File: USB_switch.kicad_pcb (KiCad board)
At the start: 2 copper layers, 29 x 44 mm, 20 parts, among them Q1 Q_PMOS_GSD, SW1 SW_SPDT

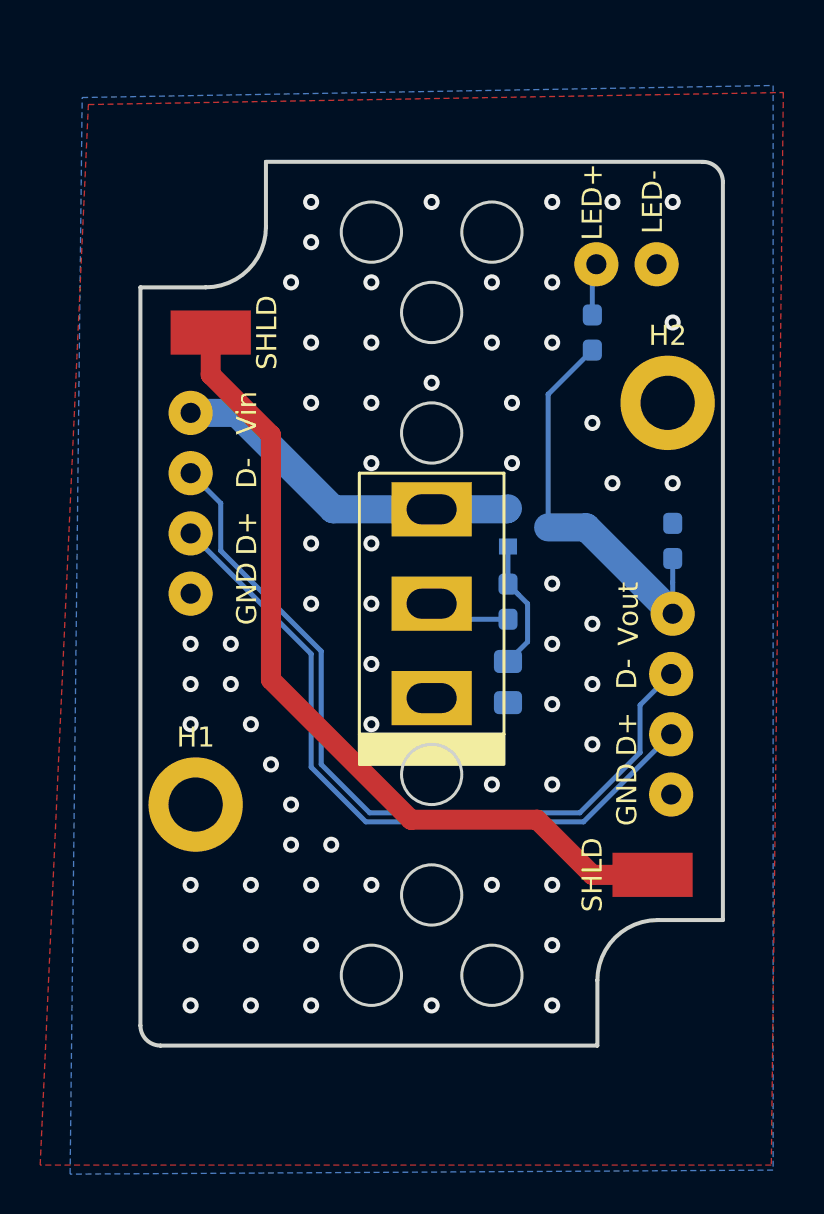
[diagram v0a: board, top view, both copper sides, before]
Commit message: Routing done with USB connector.
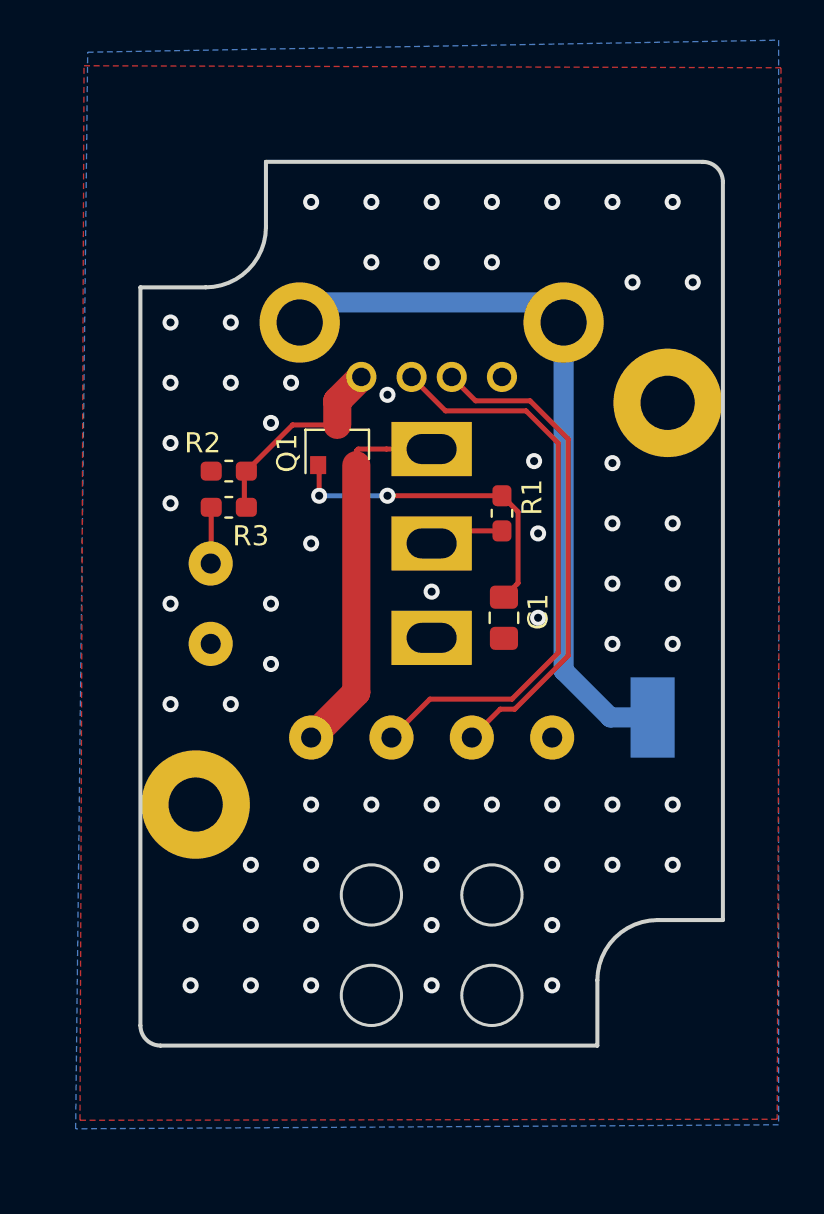
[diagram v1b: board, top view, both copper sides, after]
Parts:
- removed W11: SHLD, Pads:wirepad_SMD_2.2x4mm
- removed W2: Vout, Pads:wirepad_hole_2.2x1mm
- removed W3: GND, Pads:wirepad_hole_2.2x1mm
- removed W4: D+, Pads:wirepad_hole_2.2x1mm
- removed W5: D-, Pads:wirepad_hole_2.2x1mm
- added J1: USB_A, Connectors_custom:USB_A_Receptacle_Horizontal, B.Cu at (100.0, 86.0)
- C1, Q1, R1, R2, R3: moved to F.Cu
- H1, H2: footprint MountingHole:MountingHole_2.7mm_M2.5_DIN965_Pad -> MountingHole:MountingHole_2.7mm_M2.5_Pad
- SW1, W1, W10, W12, W6, W7, W8, W9: moved to B.Cu
- moved W12 29.2 mm to (111.0, 105.7), turned to 0 degrees
- moved W10 29.2 mm to (89.0, 102.0), turned to 270 degrees
- moved W9 24.3 mm to (89.0, 98.0), turned to 270 degrees
- moved R2 22.4 mm to (89.9, 93.4), turned to 180 degrees
- moved R3 20.1 mm to (89.9, 95.2), turned to 180 degrees
- moved W6 19.4 mm to (106.0, 106.7), turned to 0 degrees
- moved W7 17.3 mm to (102.0, 106.7), turned to 0 degrees
- moved W1 17.2 mm to (94.0, 106.7), turned to 0 degrees
- moved W8 16.5 mm to (98.0, 106.7), turned to 0 degrees
- moved Q1 10.3 mm to (95.3, 92.1), turned to 90 degrees
- moved R1 4.41 mm to (103.5, 95.5)
- moved C1 3.21 mm to (103.6, 100.7)
- moved SW1 3.00 mm to (100.0, 97.0), turned to 180 degrees
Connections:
- net Net-(Q1-Pad3) renamed Vout
- SW1 pad 1: (no net) -> GND
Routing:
- net Net-(J1-Pad2): track 39.9 -> 29.2 mm
- net Net-(J1-Pad3): track 35.0 -> 24.4 mm
- net Vout: track 20.5 -> 10.2 mm
- net Net-(C1-Pad1): track 6.53 -> 16.3 mm, vias 0 -> 2
- net Net-(J1-Pad5): track 41.6 -> 36.9 mm
- net Net-(Q1-Pad2): track 17.8 -> 19.0 mm
- net GND: vias 63 -> 61
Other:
- outline, holes or cut-outs redrawn
